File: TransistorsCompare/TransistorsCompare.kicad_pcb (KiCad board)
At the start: 2 copper layers, 59.9 x 40.1 mm, 14 parts, among them J1 Conn_01x02_Socket, J2 Conn_01x02_Socket, J3 NPN, J4 NPN, J5 Conn_01x01_MountingPin, J6 Conn_01x01_MountingPin, U1 TL084

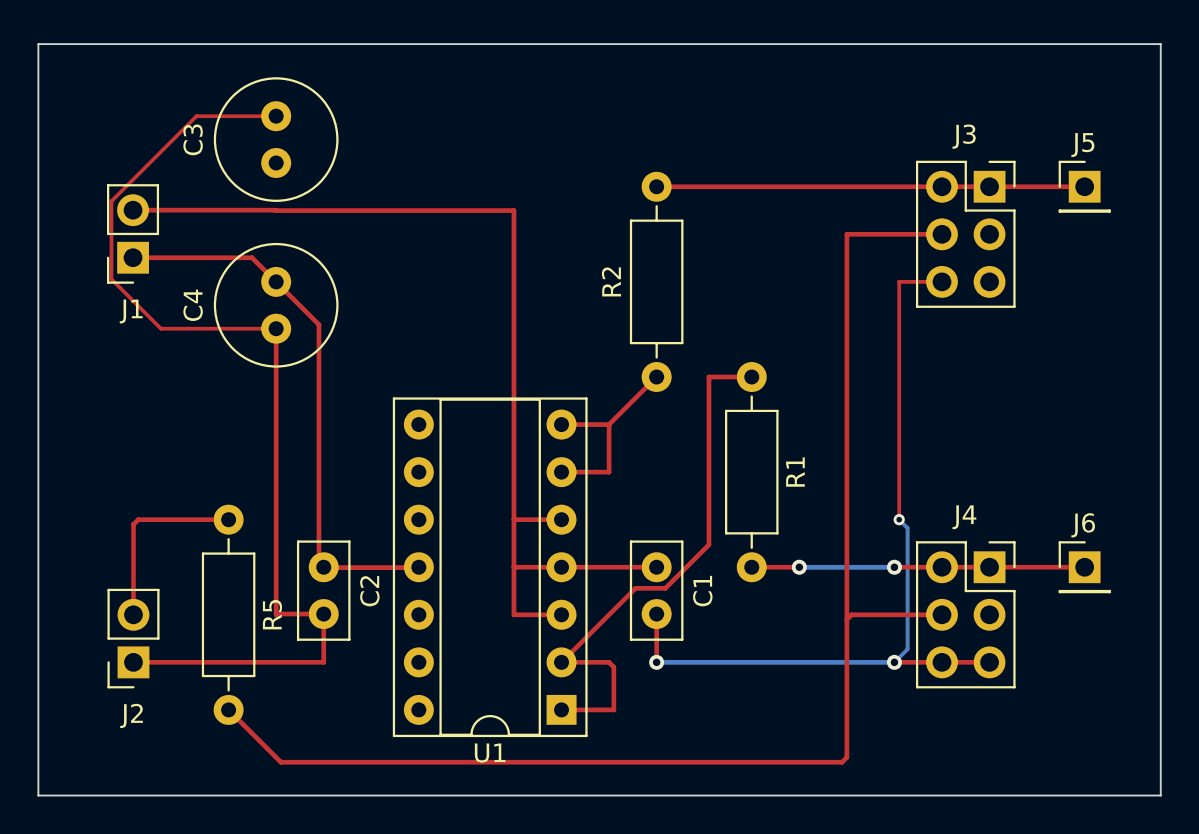
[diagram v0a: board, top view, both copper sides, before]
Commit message: fix : all thrue one AOP
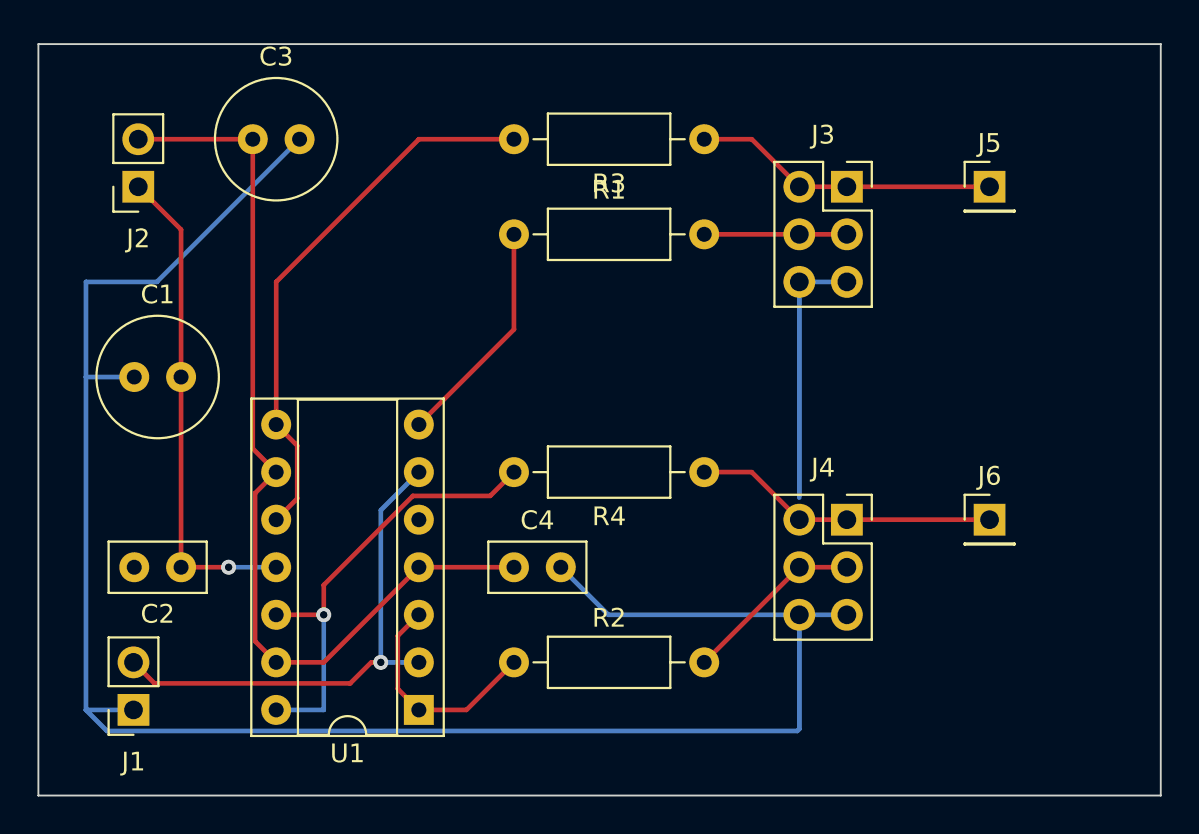
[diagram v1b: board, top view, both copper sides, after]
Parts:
- removed R5: 1.2k, Resistor_THT:R_Axial_DIN0207_L6.3mm_D2.5mm_P10.16mm_Horizontal
- added R3: 220, Resistor_THT:R_Axial_DIN0207_L6.3mm_D2.5mm_P10.16mm_Horizontal, F.Cu at (137.2, 81.3)
- added R4: 220, Resistor_THT:R_Axial_DIN0207_L6.3mm_D2.5mm_P10.16mm_Horizontal, F.Cu at (137.2, 99.1)
- C1: value 10n -> 2.2u; footprint Capacitor_THT:C_Disc_D5.0mm_W2.5mm_P2.50mm -> Capacitor_THT:C_Radial_D6.3mm_H5.0mm_P2.50mm
- C4: value 2.2u -> 10n; footprint Capacitor_THT:C_Radial_D6.3mm_H5.0mm_P2.50mm -> Capacitor_THT:C_Disc_D5.0mm_W2.5mm_P2.50mm
- J3, J4: value NPN -> Conn_02x03_Odd_Even
- J5, J6: value Conn_01x01_MountingPin -> Conn_01x01
- R1, R2: value 220 -> 1.2k
- moved C1 29.7 mm to (106.7, 94.0), turned to 0 degrees
- moved J2 25.4 mm to (106.9, 83.8)
- moved J1 24.2 mm to (106.7, 111.8)
- moved C4 18.0 mm to (127.0, 104.1), turned to 0 degrees
- moved R2 17.0 mm to (127.0, 109.2), turned to 0 degrees
- moved R1 14.8 mm to (127.0, 86.4), turned to 0 degrees
- moved J4 8.03 mm to (144.8, 101.6)
- moved C2 7.62 mm to (109.2, 104.1), turned to 180 degrees
- moved J3 7.62 mm to (144.8, 83.8)
- moved U1 7.62 mm to (121.9, 111.8)
- moved J6 5.68 mm to (152.4, 101.6)
- moved J5 5.08 mm to (152.4, 83.8)
- moved C3 1.78 mm to (113.0, 81.3), turned to 0 degrees
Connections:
- C1 pad 1: /Vcc -> GND
- C1 pad 2: GND -> /Vee
- C4 pad 1: GND -> /Vcc
- C4 pad 2: /Vee -> GND
- J1 pad 1: /Vee -> GND
- J1 pad 2: /Vcc -> /Signal
- J2 pad 1: GND -> /Vee
- J2 pad 2: Net-(J2-Pin_2) -> /Vcc
- J3 pad 3: /Signal -> Net-(J3-Pin_3)
- J3 pad 4: /Signal -> Net-(J3-Pin_3)
- J4 pad 3: /Signal -> Net-(J4-Pin_3)
- J4 pad 4: /Signal -> Net-(J4-Pin_3)
- R1 pad 1: Net-(U1A--) -> Net-(U1B-+)
- R1 pad 2: Net-(J4-Pin_1) -> Net-(J3-Pin_3)
- R2 pad 1: Net-(U1B--) -> Net-(U1A-+)
- R2 pad 2: Net-(J3-Pin_1) -> Net-(J4-Pin_3)
- U1 pad 1: Net-(U1A--) -> Net-(U1A-+)
- U1 pad 10: (no net) -> Net-(U1C-+)
- U1 pad 12: (no net) -> Net-(U1D-+)
- U1 pad 13: (no net) -> /Vcc
- U1 pad 14: (no net) -> Net-(U1D-+)
- U1 pad 2: Net-(U1A--) -> /Signal
- U1 pad 3: /Vcc -> Net-(U1A-+)
- U1 pad 5: /Vcc -> Net-(U1B-+)
- U1 pad 6: Net-(U1B--) -> /Signal
- U1 pad 7: Net-(U1B--) -> Net-(U1B-+)
- U1 pad 8: (no net) -> Net-(U1C-+)
- U1 pad 9: (no net) -> /Vcc
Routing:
- net /Signal: track 72.5 -> 27.2 mm, vias 0 -> 1
- net Net-(U1A--): track 29.7 -> 0.00 mm
- net Net-(U1C-+): track 0.00 -> 29.5 mm
- net Net-(U1D-+): track 0.00 -> 24.4 mm, vias 0 -> 2
- net GND: track 98.7 -> 117.7 mm, vias 3 -> 0
- net Net-(U1B-+): track 0.00 -> 12.3 mm
- net Net-(U1A-+): track 0.00 -> 12.1 mm
- net Net-(U1B--): track 11.2 -> 0.00 mm
- net Net-(J2-Pin_2): track 10.0 -> 0.00 mm
- net Net-(J4-Pin_3): track 0.00 -> 9.72 mm
- net Net-(J3-Pin_3): track 0.00 -> 7.62 mm
- net Net-(J3-Pin_1): track 22.9 -> 16.3 mm
- net /Vcc: track 54.6 -> 50.3 mm
- net /Vee: track 29.7 -> 26.3 mm, vias 0 -> 1
- net Net-(J4-Pin_1): track 17.8 -> 16.3 mm, vias 2 -> 0

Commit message: T compare
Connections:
- R1 pad 1: Net-(U1B-+) -> Net-(U1B--)
- R2 pad 1: Net-(U1A-+) -> Net-(U1A--)
- R3 pad 2: Net-(U1C-+) -> Net-(U1C--)
- R4 pad 2: Net-(U1D-+) -> Net-(U1D--)
- U1 pad 1: Net-(U1A-+) -> Net-(U1A--)
- U1 pad 10: Net-(U1C-+) -> /Vcc
- U1 pad 12: Net-(U1D-+) -> /Vcc
- U1 pad 13: /Vcc -> Net-(U1D--)
- U1 pad 14: Net-(U1D-+) -> Net-(U1D--)
- U1 pad 2: /Signal -> Net-(U1A--)
- U1 pad 3: Net-(U1A-+) -> /Signal
- U1 pad 5: Net-(U1B-+) -> /Signal
- U1 pad 6: /Signal -> Net-(U1B--)
- U1 pad 7: Net-(U1B-+) -> Net-(U1B--)
- U1 pad 8: Net-(U1C-+) -> Net-(U1C--)
- U1 pad 9: /Vcc -> Net-(U1C--)
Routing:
- net Net-(U1C-+): track 29.5 -> 0.00 mm
- net Net-(U1C--): track 0.00 -> 24.5 mm, vias 0 -> 2
- net Net-(U1D-+): track 24.4 -> 0.00 mm, vias 2 -> 0
- net Net-(U1D--): track 0.00 -> 21.1 mm, vias 0 -> 2
- net GND: track 117.7 -> 134.6 mm
- net Net-(U1B--): track 0.00 -> 14.8 mm
- net Net-(U1B-+): track 12.3 -> 0.00 mm
- net Net-(U1A-+): track 12.1 -> 0.00 mm
- net /Signal: track 27.2 -> 38.0 mm, vias 1 -> 2
- net Net-(U1A--): track 0.00 -> 7.62 mm
- net /Vcc: track 50.3 -> 48.8 mm
